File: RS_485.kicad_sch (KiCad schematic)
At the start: 17 parts, among them IC1 MAX485ESA+T

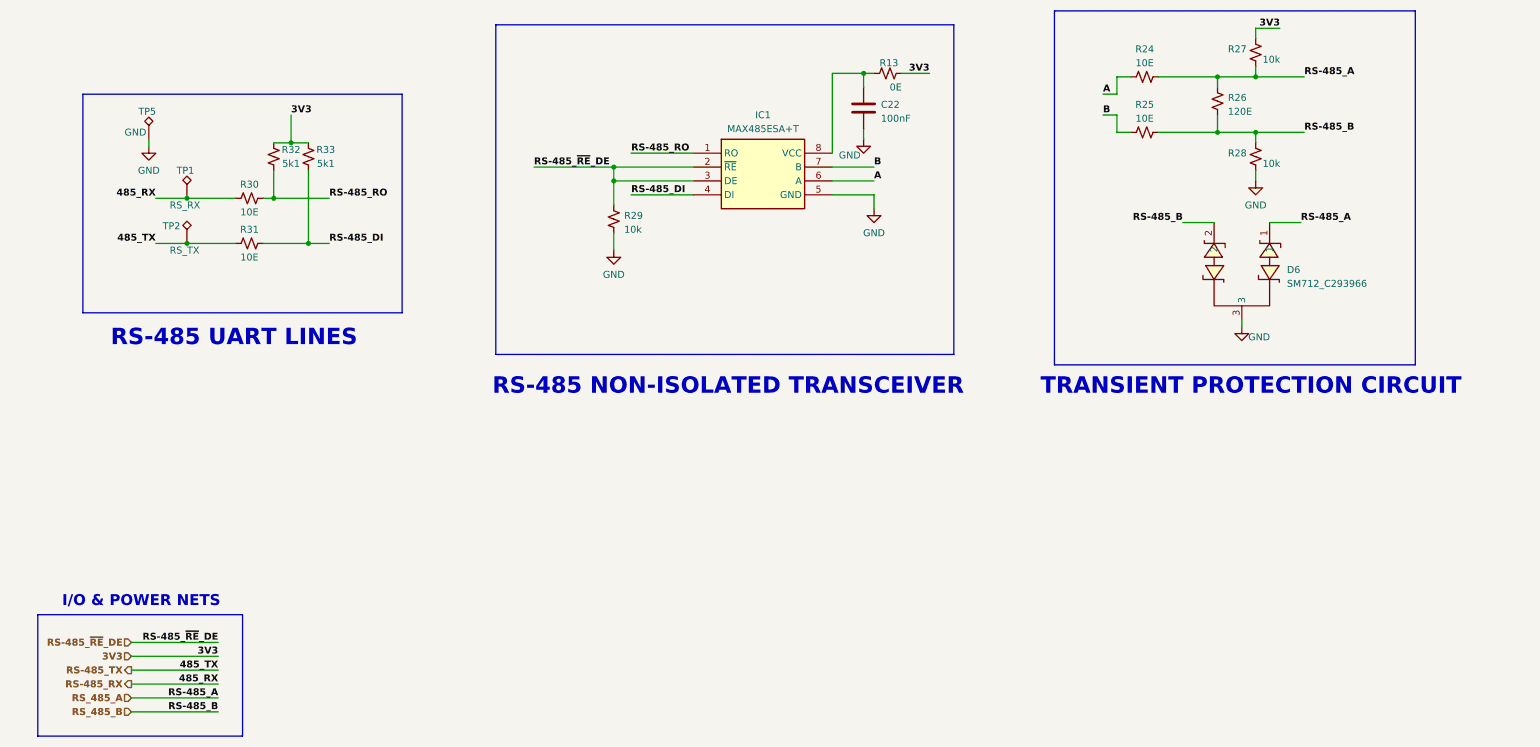
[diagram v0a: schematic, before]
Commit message: Changes CH340 schematic
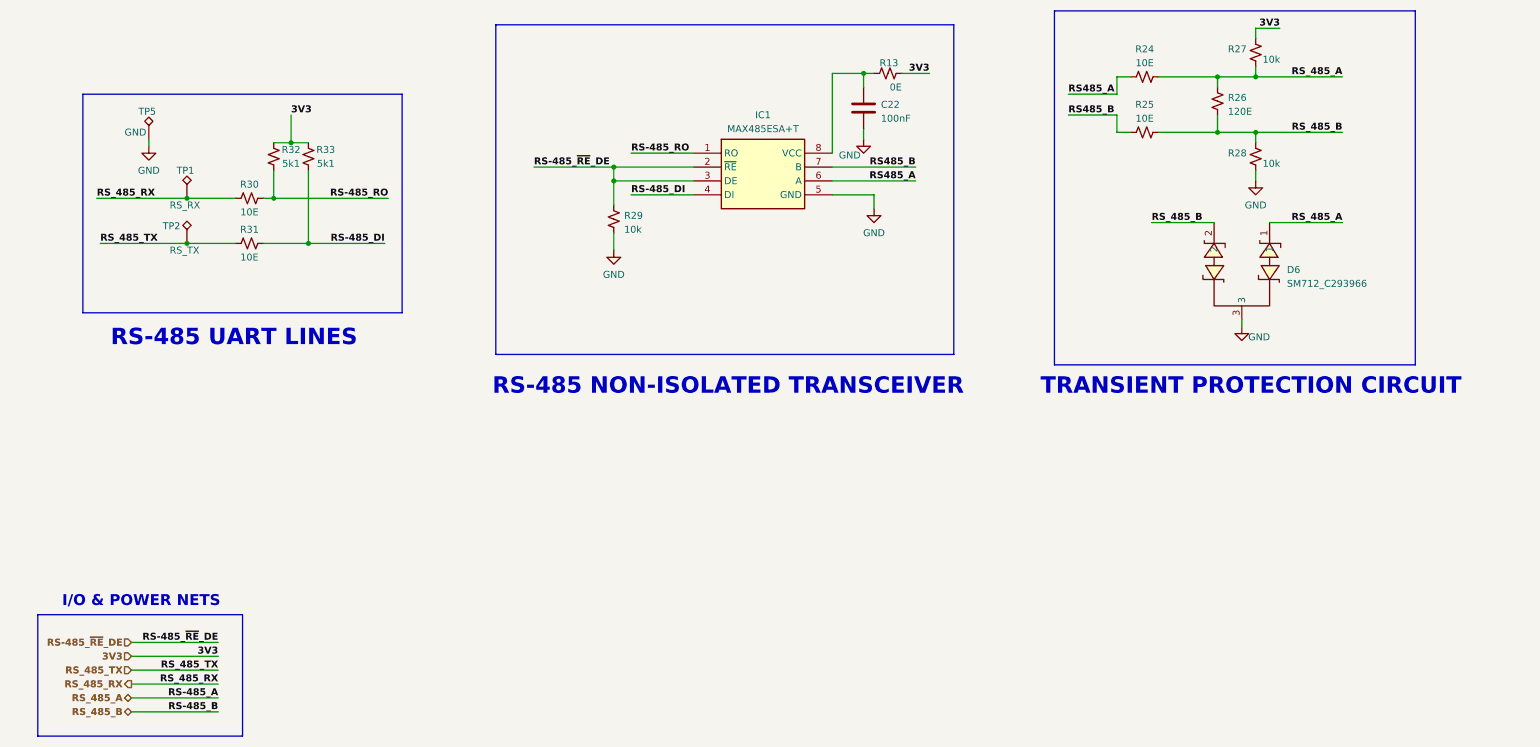
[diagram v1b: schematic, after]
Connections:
- net A renamed RS485_A
- net B renamed RS485_B
- net RS-485_RX renamed RS_485_RX
- net RS-485_TX renamed RS_485_TX
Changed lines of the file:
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@@
     (stroke (width 0) (type default))
   )
-  (wire (pts (xy 172.72 90.17) (xy 165.1 90.17))
+  (wire (pts (xy 180.34 90.17) (xy 165.1 90.17))
     (stroke (width 0) (type default))
   )
@@
     (stroke (width 0) (type default))
   )
-  (wire (pts (xy 234.95 97.79) (xy 229.235 97.79))
+  (wire (pts (xy 234.95 97.79) (xy 223.52 97.79))
     (stroke (width 0) (type default))
   )
@@
     (stroke (width 1) (type default) (color 72 72 72 1))
   )
-  (wire (pts (xy 172.72 87.63) (xy 165.1 87.63))
+  (wire (pts (xy 180.34 87.63) (xy 165.1 87.63))
     (stroke (width 0) (type default))
   )
@@
     (stroke (width 0) (type default))
   )
-  (wire (pts (xy 242.57 81.28) (xy 251.46 81.28))
+  (wire (pts (xy 242.57 81.28) (xy 258.445 81.28))
     (stroke (width 0) (type default))
   )
@@
     (stroke (width 1) (type default) (color 72 72 72 1))
   )
-  (wire (pts (xy 214.63 74.295) (xy 217.17 74.295))
-    (stroke (width 0) (type default))
-  )
-  (wire (pts (xy 242.57 71.12) (xy 251.46 71.12))
+  (wire (pts (xy 208.28 74.295) (xy 217.17 74.295))
+    (stroke (width 0) (type default))
+  )
+  (wire (pts (xy 242.57 71.12) (xy 258.445 71.12))
     (stroke (width 0) (type default))
   )
@@
     (stroke (width 1) (type default) (color 72 72 72 1))
   )
-  (wire (pts (xy 73.025 93.345) (xy 62.865 93.345))
+  (wire (pts (xy 83.82 93.345) (xy 62.865 93.345))
     (stroke (width 0) (type default))
   )
@@
     (stroke (width 0.5) (type default) (color 0 0 255 1))
   )
-  (wire (pts (xy 214.63 78.105) (xy 217.17 78.105))
+  (wire (pts (xy 208.28 78.105) (xy 217.17 78.105))
     (stroke (width 0) (type default))
   )
@@
     (stroke (width 0) (type default))
   )
-  (wire (pts (xy 41.275 101.6) (xy 46.99 101.6))
-    (stroke (width 0) (type default))
-  )
-  (wire (pts (xy 41.275 93.345) (xy 46.99 93.345))
-    (stroke (width 0) (type default))
-  )
-  (wire (pts (xy 69.215 101.6) (xy 73.025 101.6))
+  (wire (pts (xy 31.115 101.6) (xy 46.99 101.6))
+    (stroke (width 0) (type default))
+  )
+  (wire (pts (xy 30.48 93.345) (xy 46.99 93.345))
+    (stroke (width 0) (type default))
+  )
+  (wire (pts (xy 69.215 101.6) (xy 83.185 101.6))
     (stroke (width 0) (type default))
   )
@@
     (stroke (width 0.5) (type default) (color 0 0 0 1))
   )
-  (wire (pts (xy 250.825 97.79) (xy 245.11 97.79))
+  (wire (pts (xy 258.445 97.79) (xy 245.11 97.79))
     (stroke (width 0) (type default))
   )
@@
     (effects (font (size 3 3) bold (color 255 0 0 1)) (justify left bottom))
   )
-  (label "485_TX" (at 41.275 101.6 180) (fields_autoplaced)
-    (effects (font (size 1.27 1.27) (thickness 0.254) bold (color 0 0 255 1)) (justify right bottom))
-  )
-  (label "RS-485_A" (at 250.825 97.79 0) (fields_autoplaced)
-    (effects (font (size 1.27 1.27) (thickness 0.254) bold (color 0 0 0 1)) (justify left bottom))
+  (label "RS_485_A" (at 258.445 97.79 180) (fields_autoplaced)
+    (effects (font (size 1.27 1.27) (thickness 0.254) bold (color 0 0 0 1)) (justify right bottom))
   )
   (label "3V3" (at 52.705 177.165 180) (fields_autoplaced)
@@
     (effects (font (size 1.27 1.27) (thickness 0.254) bold (color 0 0 0 1)) (justify right bottom))
   )
-  (label "RS-485_B" (at 251.46 81.28 0) (fields_autoplaced)
-    (effects (font (size 1.27 1.27) (thickness 0.254) bold (color 0 0 0 1)) (justify left bottom))
+  (label "RS_485_B" (at 258.445 81.28 180) (fields_autoplaced)
+    (effects (font (size 1.27 1.27) (thickness 0.254) bold (color 0 0 0 1)) (justify right bottom))
   )
   (label "3V3" (at 182.88 70.485 180) (fields_autoplaced)
     (effects (font (size 1.27 1.27) (thickness 0.254) bold (color 255 0 0 1)) (justify right bottom))
   )
-  (label "RS-485_RO" (at 73.025 93.345 0) (fields_autoplaced)
-    (effects (font (size 1.27 1.27) bold (color 0 0 255 1)) (justify left bottom))
-  )
-  (label "RS-485_DI" (at 73.025 101.6 0) (fields_autoplaced)
-    (effects (font (size 1.27 1.27) bold (color 0 0 255 1)) (justify left bottom))
-  )
-  (label "485_RX" (at 52.705 182.245 180) (fields_autoplaced)
+  (label "RS_485_TX" (at 31.115 101.6 0) (fields_autoplaced)
+    (effects (font (size 1.27 1.27) (thickness 0.254) bold (color 0 0 255 1)) (justify left bottom))
+  )
+  (label "RS-485_RO" (at 83.82 93.345 180) (fields_autoplaced)
+    (effects (font (size 1.27 1.27) bold (color 0 0 255 1)) (justify right bottom))
+  )
+  (label "RS-485_DI" (at 83.185 101.6 180) (fields_autoplaced)
+    (effects (font (size 1.27 1.27) bold (color 0 0 255 1)) (justify right bottom))
+  )
+  (label "RS_485_RX" (at 52.705 182.245 180) (fields_autoplaced)
     (effects (font (size 1.27 1.27) (thickness 0.254) bold (color 0 0 255 1)) (justify right bottom))
   )
@@
     (effects (font (size 1.27 1.27) bold (color 0 194 0 1)) (justify left bottom))
   )
-  (label "B" (at 214.63 78.105 0) (fields_autoplaced)
-    (effects (font (size 1.27 1.27) bold (color 0 0 255 1)) (justify left bottom))
-  )
-  (label "A" (at 172.72 90.17 0) (fields_autoplaced)
-    (effects (font (size 1.27 1.27) bold (color 0 0 255 1)) (justify left bottom))
-  )
-  (label "B" (at 172.72 87.63 0) (fields_autoplaced)
-    (effects (font (size 1.27 1.27) bold (color 0 0 255 1)) (justify left bottom))
-  )
-  (label "485_TX" (at 52.705 179.705 180) (fields_autoplaced)
+  (label "RS485_B" (at 180.34 87.63 180) (fields_autoplaced)
+    (effects (font (size 1.27 1.27) bold (color 0 0 255 1)) (justify right bottom))
+  )
+  (label "RS_485_TX" (at 52.705 179.705 180) (fields_autoplaced)
     (effects (font (size 1.27 1.27) (thickness 0.254) bold (color 0 0 255 1)) (justify right bottom))
   )
-  (label "RS-485_A" (at 251.46 71.12 0) (fields_autoplaced)
-    (effects (font (size 1.27 1.27) (thickness 0.254) bold (color 0 0 0 1)) (justify left bottom))
+  (label "RS_485_A" (at 258.445 71.12 180) (fields_autoplaced)
+    (effects (font (size 1.27 1.27) (thickness 0.254) bold (color 0 0 0 1)) (justify right bottom))
   )
   (label "RS-485_DI" (at 128.27 92.71 0) (fields_autoplaced)
@@
     (effects (font (size 1.27 1.27) (thickness 0.254) bold (color 0 0 0 1)) (justify right bottom))
   )
+  (label "RS485_A" (at 208.28 74.295 0) (fields_autoplaced)
+    (effects (font (size 1.27 1.27) bold (color 0 0 255 1)) (justify left bottom))
+  )
   (label "RS-485_~{RE}_DE" (at 52.705 174.625 180) (fields_autoplaced)
     (effects (font (size 1.27 1.27) bold (color 0 194 0 1)) (justify right bottom))
   )
+  (label "RS_485_RX" (at 30.48 93.345 0) (fields_autoplaced)
+    (effects (font (size 1.27 1.27) (thickness 0.254) bold (color 0 0 255 1)) (justify left bottom))
+  )
   (label "3V3" (at 247.015 62.23 180) (fields_autoplaced)
     (effects (font (size 1.27 1.27) (thickness 0.254) bold (color 255 0 0 1)) (justify right bottom))
@@
     (effects (font (size 1.27 1.27) bold (color 0 0 255 1)) (justify left bottom))
   )
+  (label "RS485_B" (at 208.28 78.105 0) (fields_autoplaced)
+    (effects (font (size 1.27 1.27) bold (color 0 0 255 1)) (justify left bottom))
+  )
   (label "3V3" (at 66.04 78.105 0) (fields_autoplaced)
     (effects (font (size 1.27 1.27) (thickness 0.254) bold (color 255 0 0 1)) (justify left bottom))
   )
-  (label "A" (at 214.63 74.295 0) (fields_autoplaced)
-    (effects (font (size 1.27 1.27) bold (color 0 0 255 1)) (justify left bottom))
-  )
-  (label "485_RX" (at 41.275 93.345 180) (fields_autoplaced)
-    (effects (font (size 1.27 1.27) (thickness 0.254) bold (color 0 0 255 1)) (justify right bottom))
-  )
-  (label "RS-485_B" (at 229.235 97.79 180) (fields_autoplaced)
-    (effects (font (size 1.27 1.27) (thickness 0.254) bold (color 0 0 0 1)) (justify right bottom))
-  )
-  (hierarchical_label "RS-485_TX" (shape output) (at 36.83 179.705 180) (fields_autoplaced)
+  (label "RS485_A" (at 180.34 90.17 180) (fields_autoplaced)
+    (effects (font (size 1.27 1.27) bold (color 0 0 255 1)) (justify right bottom))
+  )
+  (label "RS_485_B" (at 223.52 97.79 0) (fields_autoplaced)
+    (effects (font (size 1.27 1.27) (thickness 0.254) bold (color 0 0 0 1)) (justify left bottom))
+  )
+  (hierarchical_label "RS_485_TX" (shape input) (at 36.83 179.705 180) (fields_autoplaced)
     (effects (font (size 1.27 1.27) bold (color 0 0 255 1)) (justify right))
   )
-  (hierarchical_label "RS_485_A" (shape input) (at 36.83 184.785 180) (fields_autoplaced)
+  (hierarchical_label "RS_485_A" (shape bidirectional) (at 36.83 184.785 180) (fields_autoplaced)
     (effects (font (size 1.27 1.27) bold (color 0 0 0 1)) (justify right))
   )
@@
     (effects (font (size 1.27 1.27) (thickness 0.254) bold (color 255 0 0 1)) (justify right))
   )
-  (hierarchical_label "RS-485_RX" (shape output) (at 36.83 182.245 180) (fields_autoplaced)
+  (hierarchical_label "RS_485_RX" (shape output) (at 36.83 182.245 180) (fields_autoplaced)
     (effects (font (size 1.27 1.27) bold (color 0 0 255 1)) (justify right))
   )
@@
     (effects (font (size 1.27 1.27) bold (color 0 194 0 1)) (justify right))
   )
-  (hierarchical_label "RS_485_B" (shape input) (at 36.83 187.325 180) (fields_autoplaced)
+  (hierarchical_label "RS_485_B" (shape bidirectional) (at 36.83 187.325 180) (fields_autoplaced)
     (effects (font (size 1.27 1.27) bold (color 0 0 0 1)) (justify right))
   )

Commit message: Corrected RS485 schematic
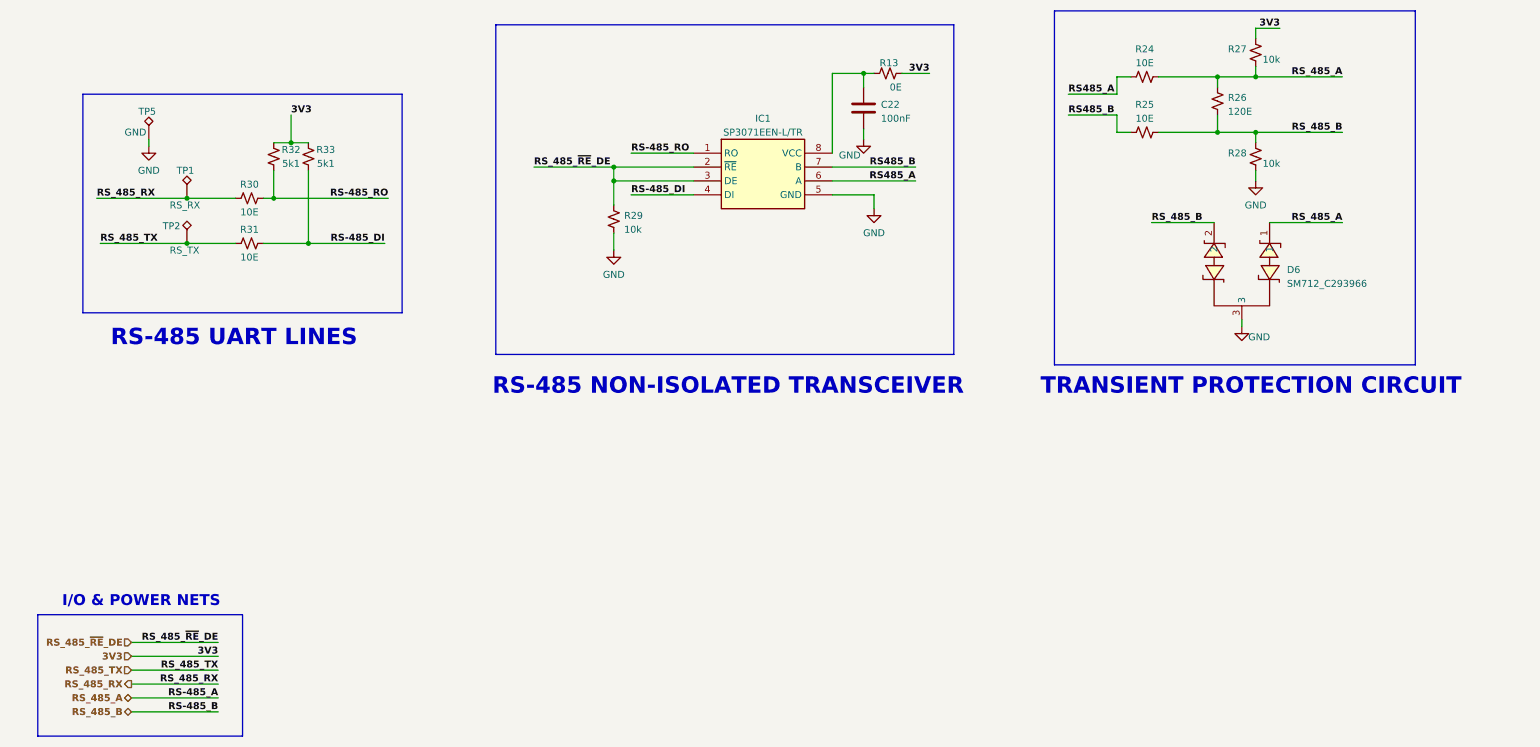
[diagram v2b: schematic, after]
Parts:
- IC1: value MAX485ESA+T -> SP3071EEN-L/TR; Manufacturer_Name Analog Devices -> MaxLinear; Manufacturer_Part_Number MAX485ESA+T -> SP3071EEN-L/TR
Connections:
- net RS-485_~{RE}_DE renamed RS_485_~{RE}_DE
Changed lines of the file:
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@@
     (effects (font (size 1.27 1.27) (thickness 0.254) bold (color 0 0 255 1)) (justify right bottom))
   )
-  (label "RS-485_~{RE}_DE" (at 110.49 87.63 0) (fields_autoplaced)
+  (label "RS_485_~{RE}_DE" (at 110.49 87.63 0) (fields_autoplaced)
     (effects (font (size 1.27 1.27) bold (color 0 194 0 1)) (justify left bottom))
   )
@@
     (effects (font (size 1.27 1.27) bold (color 0 0 255 1)) (justify left bottom))
   )
-  (label "RS-485_~{RE}_DE" (at 52.705 174.625 180) (fields_autoplaced)
-    (effects (font (size 1.27 1.27) bold (color 0 194 0 1)) (justify right bottom))
-  )
   (label "RS_485_RX" (at 30.48 93.345 0) (fields_autoplaced)
     (effects (font (size 1.27 1.27) (thickness 0.254) bold (color 0 0 255 1)) (justify left bottom))
@@
     (effects (font (size 1.27 1.27) (thickness 0.254) bold (color 255 0 0 1)) (justify left bottom))
   )
+  (label "RS_485_~{RE}_DE" (at 52.705 174.625 180) (fields_autoplaced)
+    (effects (font (size 1.27 1.27) bold (color 0 194 0 1)) (justify right bottom))
+  )
   (label "RS485_A" (at 180.34 90.17 180) (fields_autoplaced)
     (effects (font (size 1.27 1.27) bold (color 0 0 255 1)) (justify right bottom))
@@
     (effects (font (size 1.27 1.27) bold (color 0 0 255 1)) (justify right))
   )
-  (hierarchical_label "RS-485_~{RE}_DE" (shape input) (at 36.83 174.625 180) (fields_autoplaced)
+  (hierarchical_label "RS_485_~{RE}_DE" (shape input) (at 36.83 174.625 180) (fields_autoplaced)
     (effects (font (size 1.27 1.27) bold (color 0 194 0 1)) (justify right))
   )
@@
   (symbol (lib_id "ESP32-S3_DB:MAX485ESA+T") (at 139.7 85.09 0) (unit 1)
     (in_bom yes) (on_board yes) (dnp no) (fields_autoplaced)
-    (property "Reference" "IC1" (at 152.4 78.105 0)
-      (effects (font (size 1.27 1.27)))
-    )
-    (property "Value" "MAX485ESA+T" (at 152.4 80.645 0)
+    (property "Reference" "IC1" (at 152.4 78.74 0)
+      (effects (font (size 1.27 1.27)))
+    )
+    (property "Value" "SP3071EEN-L/TR" (at 152.4 81.28 0)
       (effects (font (size 1.27 1.27)))
     )
@@
       (effects (font (size 1.27 1.27)) (justify left top) hide)
     )
-    (property "Datasheet" "https://datasheets.maximintegrated.com/en/ds/MAX1487-MAX491.pdf" (at 161.29 280.01 0)
+    (property "Datasheet" "https://assets.maxlinear.com/web/documents/sipex/datasheets/sp3494.pdf" (at 161.29 280.01 0)
       (effects (font (size 1.27 1.27)) (justify left top) hide)
     )
@@
       (effects (font (size 1.27 1.27)) (justify left top) hide)
     )
-    (property "Manufacturer_Name" "Analog Devices" (at 161.29 580.01 0)
-      (effects (font (size 1.27 1.27)) (justify left top) hide)
-    )
-    (property "Manufacturer_Part_Number" "MAX485ESA+T" (at 161.29 680.01 0)
-      (effects (font (size 1.27 1.27)) (justify left top) hide)
-    )
+    (property "Manufacturer_Name" "MaxLinear" (at 161.29 580.01 0)
+      (effects (font (size 1.27 1.27)) (justify left top) hide)
+    )
+    (property "Manufacturer_Part_Number" "SP3071EEN-L/TR" (at 161.29 680.01 0)
+      (effects (font (size 1.27 1.27)) (justify left top) hide)
+    )
